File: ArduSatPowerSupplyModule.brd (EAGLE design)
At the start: 95.5 x 90.3 mm, 81 parts, among them IC1 RT9276, IC2 LTC4054, IC3 ATMEGA32U4-QFN, Q1 2N7002, Q2 BSS138 N-MOSFET, Q3 MOSFET-PCHANNELSMT2, Q4 BSS138 N-MOSFET, SW1 SWITCH-DPDT, SW2 RESET, U1 MAX17043G+U, X3 USBSF-MICROB

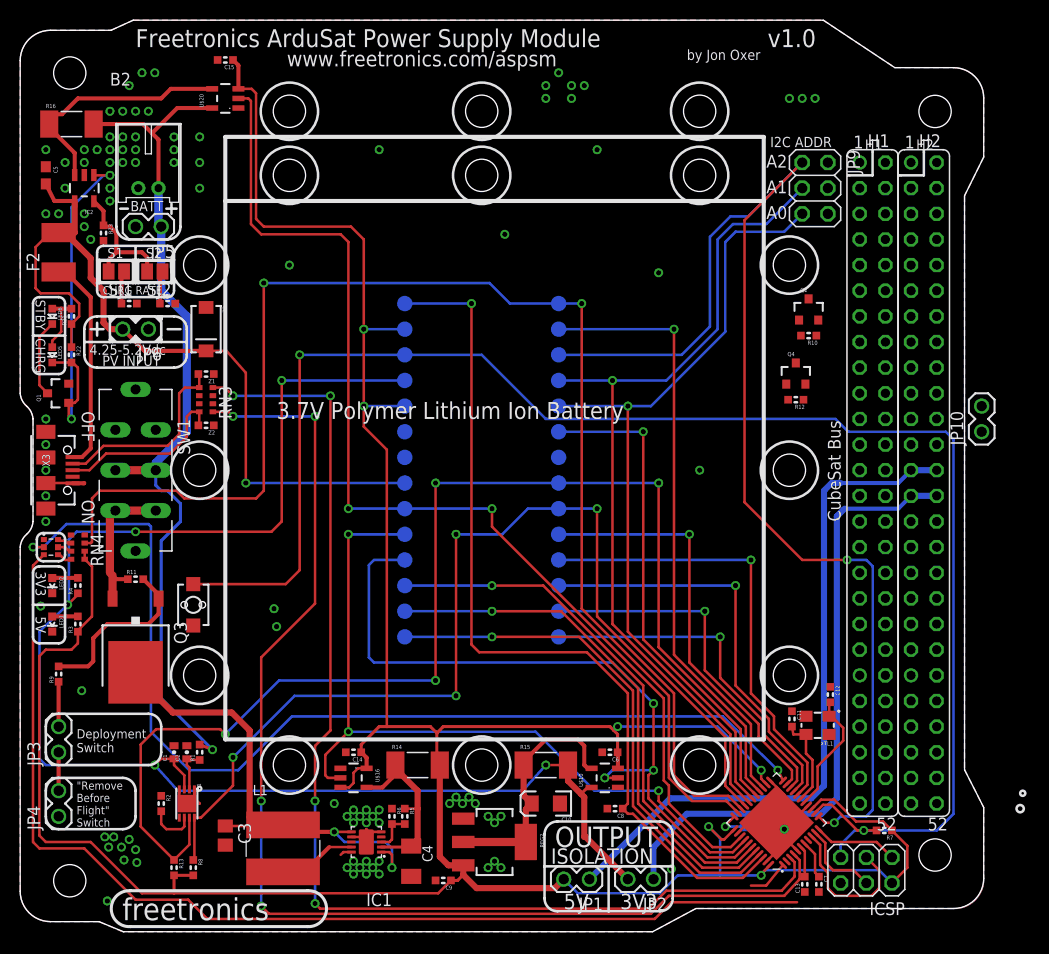
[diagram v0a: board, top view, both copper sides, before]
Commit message: Completed routing
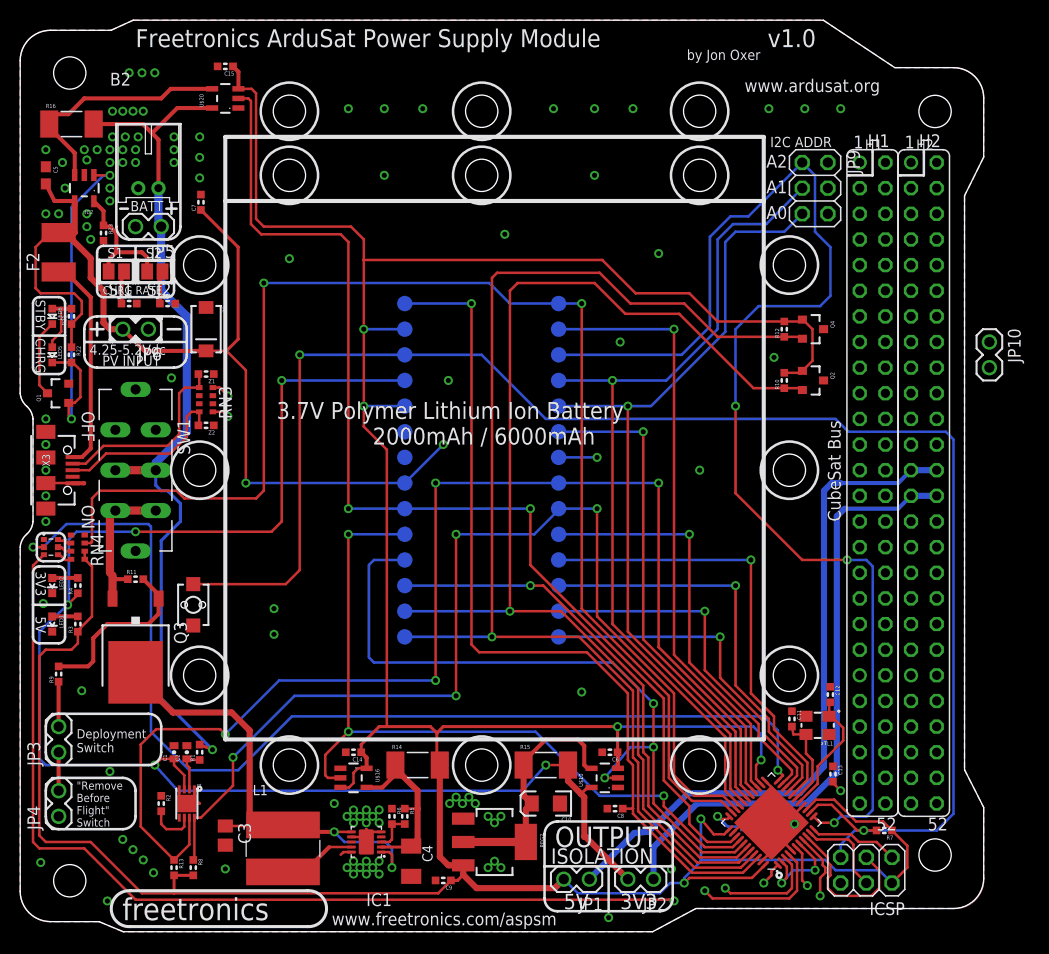
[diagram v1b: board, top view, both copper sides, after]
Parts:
- moved C7 91.2 mm to (17.9, 72.3), turned to 90 degrees
- moved C13 11.3 mm to (80.5, 15.6), turned to 270 degrees
- moved JP10 8.92 mm to (96.0, 58.4), turned to 270 degrees
- moved R12 7.08 mm to (75.7, 59.7), turned to 90 degrees
- moved Q2 7.00 mm to (78.5, 54.6), turned to 270 degrees
- moved R10 5.06 mm to (75.7, 54.6), turned to 90 degrees
- moved Q4 4.74 mm to (78.5, 59.7), turned to 270 degrees
- moved C15 0.64 mm to (20.3, 85.7)
- moved IC3 0.51 mm to (74.4, 10.8)
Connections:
- net +5V_SYS: no longer Q2.1, Q4.1, R10.2, R12.2
- net 5V_REG: now also Q2.1, Q4.1, R10.2, R12.2
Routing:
- net USBVCC: track 82.6 -> 177.3 mm, vias 1 -> 4
- net A5_SCL: track 52.3 -> 120.6 mm
- net A4_SDA: track 52.7 -> 117.2 mm
- net 5V_REG: track 310.0 -> 373.5 mm
- net D7_AIN0: track 4.15 -> 55.2 mm, vias 0 -> 2
- net RD+: track 118.9 -> 99.5 mm, vias 4 -> 2
- net RD-: track 114.0 -> 98.6 mm, vias 4 -> 2
- net 3V3: track 3.09 -> 17.4 mm, vias 0 -> 2
- net RXLED_SS: track 108.4 -> 116.2 mm, vias 0 -> 2
- net D11: track 118.9 -> 126.0 mm, vias 2 -> 3
- net GND: track 38.1 -> 43.3 mm, vias 100 -> 105
- net TX_LED: track 103.4 -> 106.0 mm
- net N$10: track 3.40 -> 5.74 mm
- net VCC_SYS: track 62.0 -> 60.5 mm
- net A0: track 110.5 -> 111.8 mm
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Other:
- board text added: "(Default)"
- board text added: "100mA"
- board text added: "2000mAh / 6000mAh"
- board text added: "200mA"
- board text added: "403mA"
- board text added: "503mA"
- board text added: "A0(CHARGE mA)"
- board text added: "A1(5V mA)"
- board text added: "A2 (3V3 mA)"
- board text added: "A3"
- board text added: "A4(I2C)"
- board text added: "A5(I2C)"
- board text added: "AREF"
- board text added: "CHARGE RATE"
- board text added: "Closed"
- board text added: "Copyright 2012 Freetronics Pty Ltd www.freetronics.com/aspsm SKU: ASPSM"
- board text added: "D0"
- board text added: "D1"
- board text added: "D10(ADDR1)"
- board text added: "D11(ADDR2)"
- board text added: "D12"
- board text added: "D13"
- board text added: "D2"
- board text added: "D3"
- board text added: "D4"
- board text added: "D5(I2C)"
- board text added: "D6(I2C)"
- board text added: "D7"
- board text added: "D8"
- board text added: "D9(ADDR0)"
- board text added: "GND"
- board text added: "HWB"
- board text added: "Open"
- board text added: "RESET"
- board text added: "Released under the TAPR Open Hardware License www.tapr.org/OHL"
- board text added: "VIN"
- board text added: "www.ardusat.org"
- board text removed: "(c) 2012 Freetronics Pty Ltd"

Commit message: Linked I2C with CubeSat bus; clearance and overlay improvements
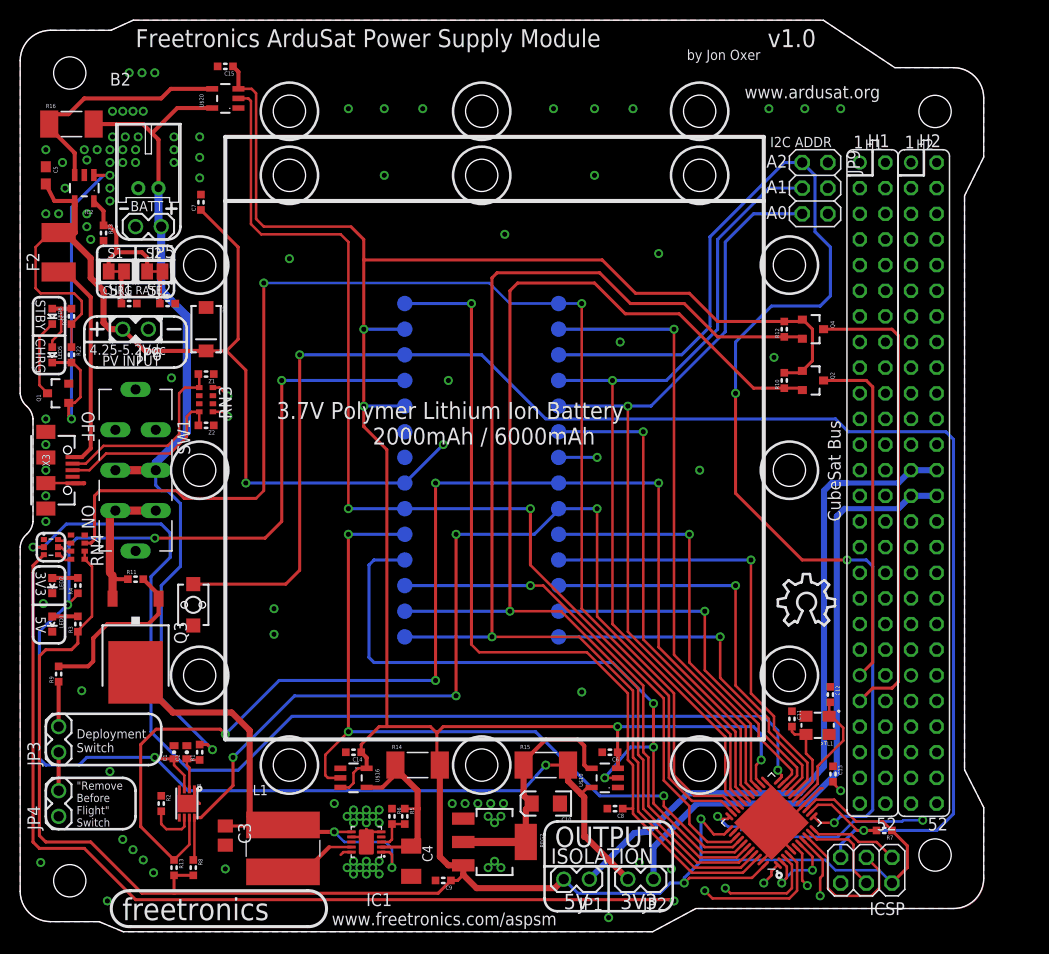
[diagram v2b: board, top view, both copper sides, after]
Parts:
- removed JP10: (no value), freetronics-master-v1:1X02
- added U$1, U$2: (no value), OSHW:OSHW_10X200_NOTEXT
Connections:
- removed net H1L41: H1.41
- removed net H1L43: H1.43
- net MGMNT_SCL: now also H1.43; no longer JP10.1
- net MGMNT_SDA: now also H1.41; no longer JP10.2
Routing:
- net MGMNT_SCL: track 0.00 -> 46.6 mm
- net MGMNT_SDA: track 0.00 -> 34.2 mm
- net GND: track 43.3 -> 64.0 mm, vias 105 -> 106
- net TX_LED: track 106.0 -> 108.2 mm
- net N$9: track 0.00 -> 1.27 mm
- net N$8: track 0.00 -> 1.27 mm
- net D11: track 126.0 -> 125.2 mm
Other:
- board text added: "1"
- board text added: "100mA 200mA 403mA 503mA (default)"
- board text added: "2"
- board text added: "51"
- board text added: "52"
- board text added: "A2(3V3 mA)"
- board text added: "A4(I2C SDA)"
- board text added: "A5(I2C SCL)"
- board text added: "ADDR0"
- board text added: "ADDR1"
- board text added: "ADDR2"
- board text added: "CUBESAT BUS"
- board text added: "D5(I2CSCL)"
- board text added: "D6(I2CSDA)"
- board text added: "D9 (ADDR0)"
- board text added: "H1-41: MGMNT_SDA H1-43: MGMNT_SCL H2-25: 5V H2-26: 5V H2-27: 3V3 H2-28: 3V3 H2-29: GND H2-30: GND H2-32: GND"
- board text added: "ROHS"
- board text added: "S1 Open Open Closed Closed"
- board text added: "S2 Open Closed Open Closed"
- board text added: "SCL"
- board text added: "SDA"
- board text removed: "(Default)"
- board text removed: "100mA"
- board text removed: "200mA"
- board text removed: "403mA"
- board text removed: "503mA"
- board text removed: "A2 (3V3 mA)"
- board text removed: "A4(I2C)"
- board text removed: "A5(I2C)"
- board text removed: "Closed"
- board text removed: "D5(I2C)"
- board text removed: "D6(I2C)"
- board text removed: "D9(ADDR0)"
- board text removed: "Open"

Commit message: Added optional I2C pull-ups on CubeSat bus side of the isolators. Changed polygon isolation to 0.012 on inner layers, 0.010 on outer. Improved spacing.
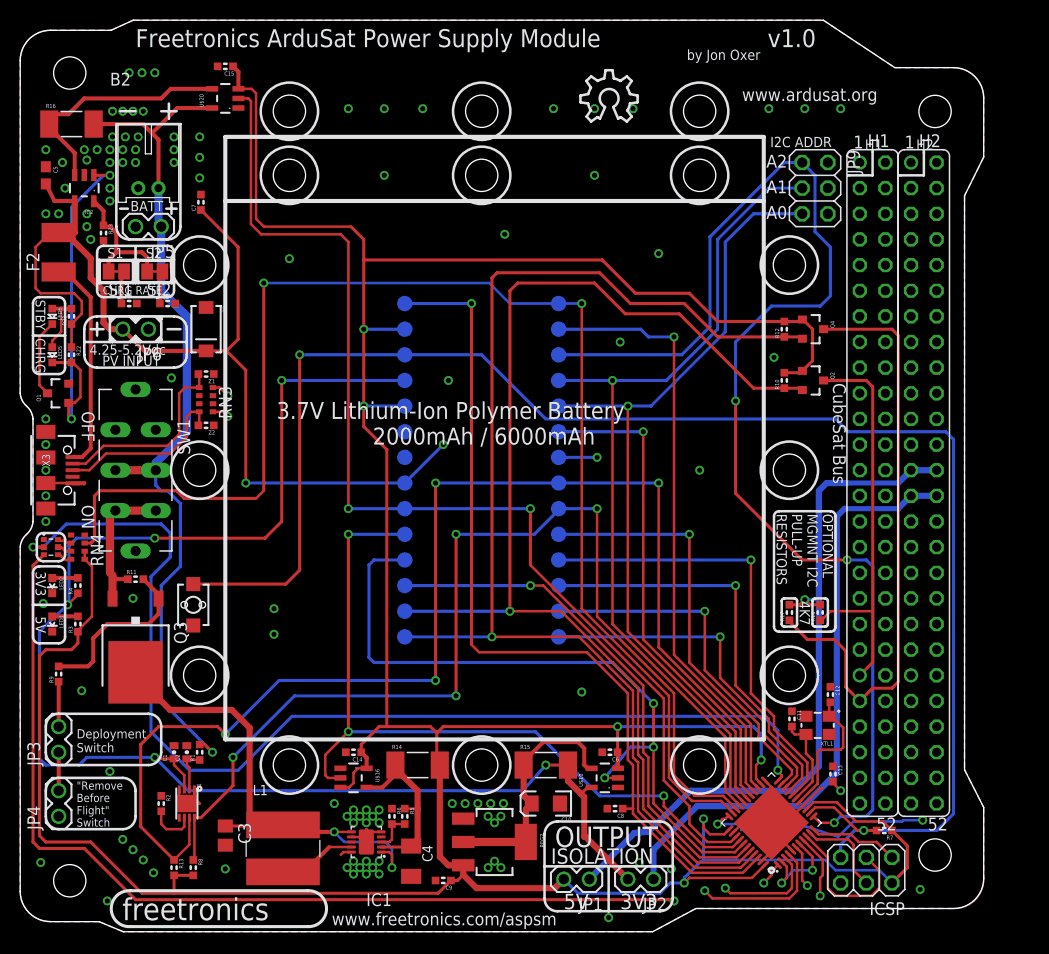
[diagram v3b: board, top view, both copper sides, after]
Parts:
- added R17, R18: 4K7 0603, freetronics-master-v1.1:0603
- moved U$2 53.6 mm to (55.5, 80.3)
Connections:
- net +5V_SYS: now also R17.2, R18.2
- net MGMNT_SCL: now also R17.1
- net MGMNT_SDA: now also R18.1
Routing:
- net MGMNT_SCL: track 46.6 -> 59.0 mm
- net GND: track 64.0 -> 71.4 mm, vias 106 -> 108
- net MGMNT_SDA: track 34.2 -> 40.0 mm
- net +5V_SYS: track 67.2 -> 72.0 mm, vias 0 -> 1
- net N$10: track 5.74 -> 4.28 mm
- net N$12: track 12.5 -> 13.6 mm
- net N$13: track 0.00 -> 0.76 mm
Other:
- board text added: "3.7V Lithium-Ion Polymer Battery"
- board text added: "4K7"
- board text added: "OPTIONAL MGMNT I2C PULL-UP RESISTORS"
- board text removed: "3.7V Polymer Lithium Ion Battery"
